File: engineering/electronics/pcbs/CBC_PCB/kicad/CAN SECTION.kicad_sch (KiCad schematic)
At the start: 44 parts, among them U25 ADM3053BRWZ-REEL7, U26 ADM3053BRWZ-REEL7, X1 8MHz, X2 8MHz

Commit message: electronics: integrate CBC PCB updates
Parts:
- C10, C11, C3, C6: symbol EasyEDA_Lib:CC0402JRNPO9BN220 -> CBC_PCB:CC0402JRNPO9BN220
- C12, C48, C49, C5, C53, C54: symbol EasyEDA_Lib:CL21A475KBQNNNE -> CBC_PCB:CL21A475KBQNNNE
- C13, C4, C47, C50, C51, C55, C56, C57: symbol EasyEDA_Lib:GRM21BR61H106KE43L -> CBC_PCB:GRM21BR61H106KE43L
- C14, C2, C52, C58: symbol EasyEDA_Lib:CC0402KRX7R7BB104 -> CBC_PCB:CC0402KRX7R7BB104
- C16, C17, C8, C9: symbol EasyEDA_Lib:GRM1555C1H221JA01D -> CBC_PCB:GRM1555C1H221JA01D
- D1, D2: symbol EasyEDA_Lib:NUP2105LT1G -> CBC_PCB:NUP2105LT1G
- H1, H2: symbol EasyEDA_Lib:PZ254V-11-02P -> CBC_PCB:PZ254V-11-02P
- L1, L2: symbol EasyEDA_Lib:ACT45B-510-2P-TF -> CBC_PCB:ACT45B-510-2P-TF
- R1, R4: symbol EasyEDA_Lib:0603WAF1200T5E -> CBC_PCB:0603WAF1200T5E
- R2, R3: symbol EasyEDA_Lib:RT0402BRD0710KL -> CBC_PCB:RT0402BRD0710KL
- R34, R35: symbol EasyEDA_Lib:RC0402FR-070RL -> CBC_PCB:RC0402FR-070RL
- U25, U26: symbol EasyEDA_Lib:ADM3053BRWZ-REEL7 -> CBC_PCB:ADM3053BRWZ-REEL7
- U3, U5: symbol EasyEDA_Lib:MCP2515T-I/ST -> CBC_PCB:MCP2515T-I/ST
- X1, X2: symbol EasyEDA_Lib:H1OEL89CSC-SUGYLC-8M -> CBC_PCB:H1OEL89CSC-SUGYLC-8M
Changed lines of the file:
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@@
 	)
 	(junction
-		(at 281.94 200.66)
-		(diameter 0)
-		(color 0 0 0 0)
-	)
-	(junction
 		(at 302.26 55.88)
 		(diameter 0)
@@
 	)
 	(junction
-		(at 266.7 64.77)
-		(diameter 0)
-		(color 0 0 0 0)
-	)
-	(junction
 		(at 57.15 74.93)
 		(diameter 0)
@@
 	(wire
 		(pts
-			(xy 266.7 64.77) (xy 261.62 64.77)
+			(xy 261.62 64.77) (xy 267.97 64.77)
 		)
 		(stroke
@@
 	(wire
 		(pts
-			(xy 267.97 64.77) (xy 266.7 64.77)
-		)
-		(stroke
-			(width 0)
-			(type default)
-		)
-	)
-	(wire
-		(pts
 			(xy 340.36 180.34) (xy 346.71 180.34)
 		)
@@
 	(wire
 		(pts
-			(xy 284.48 200.66) (xy 281.94 200.66)
-		)
-		(stroke
-			(width 0)
-			(type default)
-		)
-	)
-	(wire
-		(pts
 			(xy 283.21 194.31) (xy 288.29 194.31)
 		)
@@
 	(wire
 		(pts
-			(xy 281.94 200.66) (xy 278.13 200.66)
+			(xy 278.13 200.66) (xy 284.48 200.66)
 		)
 		(stroke
@@
 	)
 	(symbol
-		(lib_id "EasyEDA_Lib:GRM1555C1H221JA01D")
+		(lib_id "CBC_PCB:GRM1555C1H221JA01D")
 		(at 323.85 196.85 90)
 		(unit 1)
@@
 	)
 	(symbol
-		(lib_id "EasyEDA_Lib:ADM3053BRWZ-REEL7")
+		(lib_id "CBC_PCB:ADM3053BRWZ-REEL7")
 		(at 220.98 55.88 0)
 		(unit 1)
@@
 	)
 	(symbol
-		(lib_id "EasyEDA_Lib:CL21A475KBQNNNE")
+		(lib_id "CBC_PCB:CL21A475KBQNNNE")
 		(at 196.85 201.93 90)
 		(unit 1)
@@
 	)
 	(symbol
-		(lib_id "EasyEDA_Lib:GRM1555C1H221JA01D")
+		(lib_id "CBC_PCB:GRM1555C1H221JA01D")
 		(at 314.96 59.69 90)
 		(unit 1)
@@
 	)
 	(symbol
-		(lib_id "EasyEDA_Lib:H1OEL89CSC-SUGYLC-8M")
+		(lib_id "CBC_PCB:H1OEL89CSC-SUGYLC-8M")
 		(at 41.91 215.9 0)
 		(unit 1)
@@
 	)
 	(symbol
-		(lib_id "EasyEDA_Lib:0603WAF1200T5E")
+		(lib_id "CBC_PCB:0603WAF1200T5E")
 		(at 302.26 49.53 90)
 		(unit 1)
@@
 	)
 	(symbol
-		(lib_id "EasyEDA_Lib:RC0402FR-070RL")
+		(lib_id "CBC_PCB:RC0402FR-070RL")
 		(at 248.92 36.83 0)
 		(unit 1)
@@
 	)
 	(symbol
-		(lib_id "EasyEDA_Lib:GRM21BR61H106KE43L")
+		(lib_id "CBC_PCB:GRM21BR61H106KE43L")
 		(at 207.01 203.2 90)
 		(unit 1)
@@
 	)
 	(symbol
-		(lib_id "EasyEDA_Lib:H1OEL89CSC-SUGYLC-8M")
+		(lib_id "CBC_PCB:H1OEL89CSC-SUGYLC-8M")
 		(at 44.45 74.93 0)
 		(unit 1)
@@
 	)
 	(symbol
-		(lib_id "EasyEDA_Lib:RC0402FR-070RL")
+		(lib_id "CBC_PCB:RC0402FR-070RL")
 		(at 265.43 172.72 0)
 		(unit 1)
@@
 	)
 	(symbol
-		(lib_id "EasyEDA_Lib:NUP2105LT1G")
+		(lib_id "CBC_PCB:NUP2105LT1G")
 		(at 335.28 214.63 180)
 		(unit 1)
@@
 	)
 	(symbol
-		(lib_id "EasyEDA_Lib:CL21A475KBQNNNE")
+		(lib_id "CBC_PCB:CL21A475KBQNNNE")
 		(at 175.26 49.53 90)
 		(unit 1)
@@
 	)
 	(symbol
-		(lib_id "EasyEDA_Lib:ACT45B-510-2P-TF")
+		(lib_id "CBC_PCB:ACT45B-510-2P-TF")
 		(at 289.56 54.61 0)
 		(unit 1)
@@
 	)
 	(symbol
-		(lib_id "EasyEDA_Lib:CL21A475KBQNNNE")
+		(lib_id "CBC_PCB:CL21A475KBQNNNE")
 		(at 180.34 66.04 90)
 		(unit 1)
@@
 	)
 	(symbol
-		(lib_id "EasyEDA_Lib:CL21A475KBQNNNE")
+		(lib_id "CBC_PCB:CL21A475KBQNNNE")
 		(at 191.77 185.42 90)
 		(unit 1)
@@
 	)
 	(symbol
-		(lib_id "EasyEDA_Lib:GRM21BR61H106KE43L")
+		(lib_id "CBC_PCB:GRM21BR61H106KE43L")
 		(at 278.13 207.01 90)
 		(unit 1)
@@
 	)
 	(symbol
-		(lib_id "EasyEDA_Lib:NUP2105LT1G")
+		(lib_id "CBC_PCB:NUP2105LT1G")
 		(at 326.39 77.47 180)
 		(unit 1)
@@
 	)
 	(symbol
-		(lib_id "EasyEDA_Lib:0603WAF1200T5E")
+		(lib_id "CBC_PCB:0603WAF1200T5E")
 		(at 311.15 186.69 90)
 		(unit 1)
@@
 	)
 	(symbol
-		(lib_id "EasyEDA_Lib:PZ254V-11-02P")
+		(lib_id "CBC_PCB:PZ254V-11-02P")
 		(at 316.23 194.31 0)
 		(unit 1)
@@
 	)
 	(symbol
-		(lib_id "EasyEDA_Lib:PZ254V-11-02P")
+		(lib_id "CBC_PCB:PZ254V-11-02P")
 		(at 307.34 57.15 0)
 		(unit 1)
@@
 	)
 	(symbol
-		(lib_id "EasyEDA_Lib:GRM21BR61H106KE43L")
+		(lib_id "CBC_PCB:GRM21BR61H106KE43L")
 		(at 185.42 50.8 90)
 		(unit 1)
@@
 	)
 	(symbol
-		(lib_id "EasyEDA_Lib:GRM1555C1H221JA01D")
+		(lib_id "CBC_PCB:GRM1555C1H221JA01D")
 		(at 323.85 185.42 90)
 		(unit 1)
@@
 	)
 	(symbol
-		(lib_id "EasyEDA_Lib:GRM21BR61H106KE43L")
+		(lib_id "CBC_PCB:GRM21BR61H106KE43L")
 		(at 190.5 67.31 90)
 		(unit 1)
@@
 	)
 	(symbol
-		(lib_id "EasyEDA_Lib:GRM21BR61H106KE43L")
+		(lib_id "CBC_PCB:GRM21BR61H106KE43L")
 		(at 100.33 92.71 90)
 		(unit 1)
@@
 	(symbol
 		(lib_id "power:PWR_FLAG")
-		(at 311.15 191.77 0)
+		(at 311.15 191.77 90)
 		(unit 1)
 		(body_style 1)
@@
 		(fields_autoplaced yes)
 		(property "Reference" "#FLG058"
-			(at 311.15 190.5 0)
+			(at 309.88 191.77 0)
 			(hide yes)
 			(show_name no)
@@
 		)
 		(property "Value" "PWR_FLAG"
-			(at 311.15 186.69 0)
+			(at 306.07 191.77 0)
 			(hide yes)
 			(show_name no)
@@
 	)
 	(symbol
-		(lib_id "EasyEDA_Lib:CC0402KRX7R7BB104")
+		(lib_id "CBC_PCB:CC0402KRX7R7BB104")
 		(at 107.95 92.71 90)
 		(unit 1)
@@
 	)
 	(symbol
-		(lib_id "EasyEDA_Lib:CC0402JRNPO9BN220")
+		(lib_id "CBC_PCB:CC0402JRNPO9BN220")
 		(at 54.61 219.71 90)
 		(unit 1)
@@
 	)
 	(symbol
-		(lib_id "EasyEDA_Lib:CC0402JRNPO9BN220")
+		(lib_id "CBC_PCB:CC0402JRNPO9BN220")
 		(at 57.15 78.74 90)
 		(unit 1)
@@
 	)
 	(symbol
-		(lib_id "EasyEDA_Lib:CL21A475KBQNNNE")
+		(lib_id "CBC_PCB:CL21A475KBQNNNE")
 		(at 87.63 232.41 90)
 		(unit 1)
@@
 	)
 	(symbol
-		(lib_id "EasyEDA_Lib:CL21A475KBQNNNE")
+		(lib_id "CBC_PCB:CL21A475KBQNNNE")
 		(at 90.17 91.44 90)
 		(unit 1)
@@
 	)
 	(symbol
-		(lib_id "EasyEDA_Lib:GRM1555C1H221JA01D")
+		(lib_id "CBC_PCB:GRM1555C1H221JA01D")
 		(at 314.96 48.26 90)
 		(unit 1)
@@
 	)
 	(symbol
-		(lib_id "EasyEDA_Lib:MCP2515T-I/ST")
+		(lib_id "CBC_PCB:MCP2515T-I/ST")
 		(at 100.33 54.61 0)
 		(unit 1)
@@
 	)
 	(symbol
-		(lib_id "EasyEDA_Lib:MCP2515T-I/ST")
+		(lib_id "CBC_PCB:MCP2515T-I/ST")
 		(at 97.79 195.58 0)
 		(unit 1)
@@
 	)
 	(symbol
-		(lib_id "EasyEDA_Lib:GRM21BR61H106KE43L")
+		(lib_id "CBC_PCB:GRM21BR61H106KE43L")
 		(at 261.62 71.12 90)
 		(unit 1)
@@
 	)
 	(symbol
-		(lib_id "EasyEDA_Lib:RT0402BRD0710KL")
+		(lib_id "CBC_PCB:RT0402BRD0710KL")
 		(at 69.85 27.94 90)
 		(unit 1)
@@
 	)
 	(symbol
-		(lib_id "EasyEDA_Lib:CC0402KRX7R7BB104")
+		(lib_id "CBC_PCB:CC0402KRX7R7BB104")
 		(at 105.41 233.68 90)
 		(unit 1)
@@
 	)
 	(symbol
-		(lib_id "EasyEDA_Lib:CC0402KRX7R7BB104")
+		(lib_id "CBC_PCB:CC0402KRX7R7BB104")
 		(at 284.48 207.01 90)
 		(unit 1)
@@
 	)
 	(symbol
-		(lib_id "EasyEDA_Lib:RT0402BRD0710KL")
+		(lib_id "CBC_PCB:RT0402BRD0710KL")
 		(at 67.31 168.91 90)
 		(unit 1)
@@
 	)
 	(symbol
-		(lib_id "EasyEDA_Lib:CC0402JRNPO9BN220")
+		(lib_id "CBC_PCB:CC0402JRNPO9BN220")
 		(at 30.48 78.74 90)
 		(unit 1)
@@
 	)
 	(symbol
-		(lib_id "EasyEDA_Lib:GRM21BR61H106KE43L")
+		(lib_id "CBC_PCB:GRM21BR61H106KE43L")
 		(at 201.93 186.69 90)
 		(unit 1)
@@
 	)
 	(symbol
-		(lib_id "EasyEDA_Lib:GRM21BR61H106KE43L")
+		(lib_id "CBC_PCB:GRM21BR61H106KE43L")
 		(at 97.79 233.68 90)
 		(unit 1)
@@
 	)
 	(symbol
-		(lib_id "EasyEDA_Lib:ADM3053BRWZ-REEL7")
+		(lib_id "CBC_PCB:ADM3053BRWZ-REEL7")
 		(at 237.49 191.77 0)
 		(unit 1)
@@
 	)
 	(symbol
-		(lib_id "EasyEDA_Lib:CC0402KRX7R7BB104")
+		(lib_id "CBC_PCB:CC0402KRX7R7BB104")
 		(at 267.97 71.12 90)
 		(unit 1)
@@
 	)
 	(symbol
-		(lib_id "EasyEDA_Lib:CC0402JRNPO9BN220")
+		(lib_id "CBC_PCB:CC0402JRNPO9BN220")
 		(at 27.94 219.71 90)
 		(unit 1)
@@
 	)
 	(symbol
-		(lib_id "EasyEDA_Lib:ACT45B-510-2P-TF")
+		(lib_id "CBC_PCB:ACT45B-510-2P-TF")
 		(at 298.45 191.77 0)
 		(unit 1)

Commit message: electronics: update CBC PCB and crystal parts
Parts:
- X1, X2: value 8MHz -> 16MHz; footprint EasyEDA_Lib:HC-49S_L11.5-W4.7-P4.88 -> EasyEDA_Lib:CRYSTAL-SMD_L3.2-W2.5_3225-8MHZ; LCSC Part Name HC-49US 8MHZ 20PF ±20PPM -20~70°C (±30PPM) -> 16MHz ±50ppm 8pF; Manufacturer YXC(扬兴晶振) -> NDK; Manufacturer Part H1OEL89CSC-SUGYLC-8M -> NX3225GB-16MHZ-STD-CRA-2; Supplier Part C7471633 -> C481399
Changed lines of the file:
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@@
 			)
 		)
-		(property "Value" "8MHz"
+		(property "Value" "16MHz"
 			(at 41.91 219.71 0)
 			(show_name no)
@@
 			)
 		)
-		(property "Footprint" "EasyEDA_Lib:HC-49S_L11.5-W4.7-P4.88"
+		(property "Footprint" "EasyEDA_Lib:CRYSTAL-SMD_L3.2-W2.5_3225-8MHZ"
 			(at 41.91 215.9 0)
 			(hide yes)
@@
 			)
 		)
-		(property "Datasheet" "https://item.szlcsc.com/datasheet/H1OEL89CSC-SUGYLC-8M/8526929.html"
+		(property "Datasheet" "https://item.szlcsc.com/datasheet/NX3225GB-16MHZ-STD-CRA-2/489116.html"
 			(at 41.91 215.9 0)
 			(hide yes)
@@
 			)
 		)
-		(property "Description" "Type:Through Hole Crystal Oscillator Frequency:8MHz Normal temperature Frequency Tolerance:±20ppm Normal temperature Frequency Tolerance:±20ppm Load Capacitance:20pF Frequency Stability:±30ppm Frequency Stability:±30ppm Operating Temperature:-20°C~+70°C Ope"
+		(property "Description" "Frequency:16MHz Normal temperature Frequency Tolerance:±50ppm Load Capacitance:8pF Frequency Stability:±150ppm Equivalent Series Resistance(ESR):120Ω Operating Temperature:-40℃~+150℃"
 			(at 41.91 215.9 0)
 			(hide yes)
@@
 			)
 		)
-		(property "Manufacturer Part" "H1OEL89CSC-SUGYLC-8M"
+		(property "Manufacturer Part" "NX3225GB-16MHZ-STD-CRA-2"
 			(at 41.91 215.9 0)
 			(hide yes)
@@
 			)
 		)
-		(property "Manufacturer" "YXC(扬兴晶振)"
+		(property "Manufacturer" "NDK"
 			(at 41.91 215.9 0)
 			(hide yes)
@@
 			)
 		)
-		(property "Supplier Part" "C7471633"
+		(property "Supplier Part" "C481399"
 			(at 41.91 215.9 0)
 			(hide yes)
@@
 			)
 		)
-		(property "LCSC Part Name" "HC-49US 8MHZ 20PF ±20PPM -20~70°C (±30PPM)"
+		(property "LCSC Part Name" "16MHz ±50ppm 8pF"
 			(at 41.91 215.9 0)
 			(hide yes)
@@
 			)
 		)
-		(property "Value" "8MHz"
+		(property "Value" "16MHz"
 			(at 44.45 78.74 0)
 			(show_name no)
@@
 			)
 		)
-		(property "Footprint" "EasyEDA_Lib:HC-49S_L11.5-W4.7-P4.88"
+		(property "Footprint" "EasyEDA_Lib:CRYSTAL-SMD_L3.2-W2.5_3225-8MHZ"
 			(at 44.45 74.93 0)
 			(hide yes)
@@
 			)
 		)
-		(property "Datasheet" "https://item.szlcsc.com/datasheet/H1OEL89CSC-SUGYLC-8M/8526929.html"
+		(property "Datasheet" "https://item.szlcsc.com/datasheet/NX3225GB-16MHZ-STD-CRA-2/489116.html"
 			(at 44.45 74.93 0)
 			(hide yes)
@@
 			)
 		)
-		(property "Description" "Type:Through Hole Crystal Oscillator Frequency:8MHz Normal temperature Frequency Tolerance:±20ppm Normal temperature Frequency Tolerance:±20ppm Load Capacitance:20pF Frequency Stability:±30ppm Frequency Stability:±30ppm Operating Temperature:-20°C~+70°C Ope"
+		(property "Description" "Frequency:16MHz Normal temperature Frequency Tolerance:±50ppm Load Capacitance:8pF Frequency Stability:±150ppm Equivalent Series Resistance(ESR):120Ω Operating Temperature:-40℃~+150℃"
 			(at 44.45 74.93 0)
 			(hide yes)
@@
 			)
 		)
-		(property "Manufacturer Part" "H1OEL89CSC-SUGYLC-8M"
+		(property "Manufacturer Part" "NX3225GB-16MHZ-STD-CRA-2"
 			(at 44.45 74.93 0)
 			(hide yes)
@@
 			)
 		)
-		(property "Manufacturer" "YXC(扬兴晶振)"
+		(property "Manufacturer" "NDK"
 			(at 44.45 74.93 0)
 			(hide yes)
@@
 			)
 		)
-		(property "Supplier Part" "C7471633"
+		(property "Supplier Part" "C481399"
 			(at 44.45 74.93 0)
 			(hide yes)
@@
 			)
 		)
-		(property "LCSC Part Name" "HC-49US 8MHZ 20PF ±20PPM -20~70°C (±30PPM)"
+		(property "LCSC Part Name" "16MHz ±50ppm 8pF"
 			(at 44.45 74.93 0)
 			(hide yes)

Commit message: electronics: update CMAIN and CBC PCB files
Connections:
- net GND_CB is gone; now on net GND: C16.1, C17.2, C57.1, C58.1, D2.3, R35.2, U26.11 (GND2), U26.13 (GND2), U26.16 (GND2), U26.20 (GND2)
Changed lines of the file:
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@@
 			)
 		)
-		(property "Value" "GND_CB"
+		(property "Value" "GND"
 			(at 285.75 215.9 0)
 			(show_name no)
@@
 			)
 		)
-		(property "Value" "GND_CB"
+		(property "Value" "GND"
 			(at 276.86 215.9 0)
 			(show_name no)
@@
 			)
 		)
-		(property "Value" "GND_CB"
+		(property "Value" "GND"
 			(at 332.74 195.58 0)
 			(show_name no)
@@
 			)
 		)
-		(property "Value" "GND_CB"
+		(property "Value" "GND"
 			(at 331.47 231.14 0)
 			(show_name no)
@@
 			)
 		)
-		(property "Value" "GND_CB"
+		(property "Value" "GND"
 			(at 262.89 207.01 0)
 			(show_name no)
@@
 			)
 		)
-		(property "Value" "GND_CB"
+		(property "Value" "GND"
 			(at 270.51 176.53 0)
 			(show_name no)

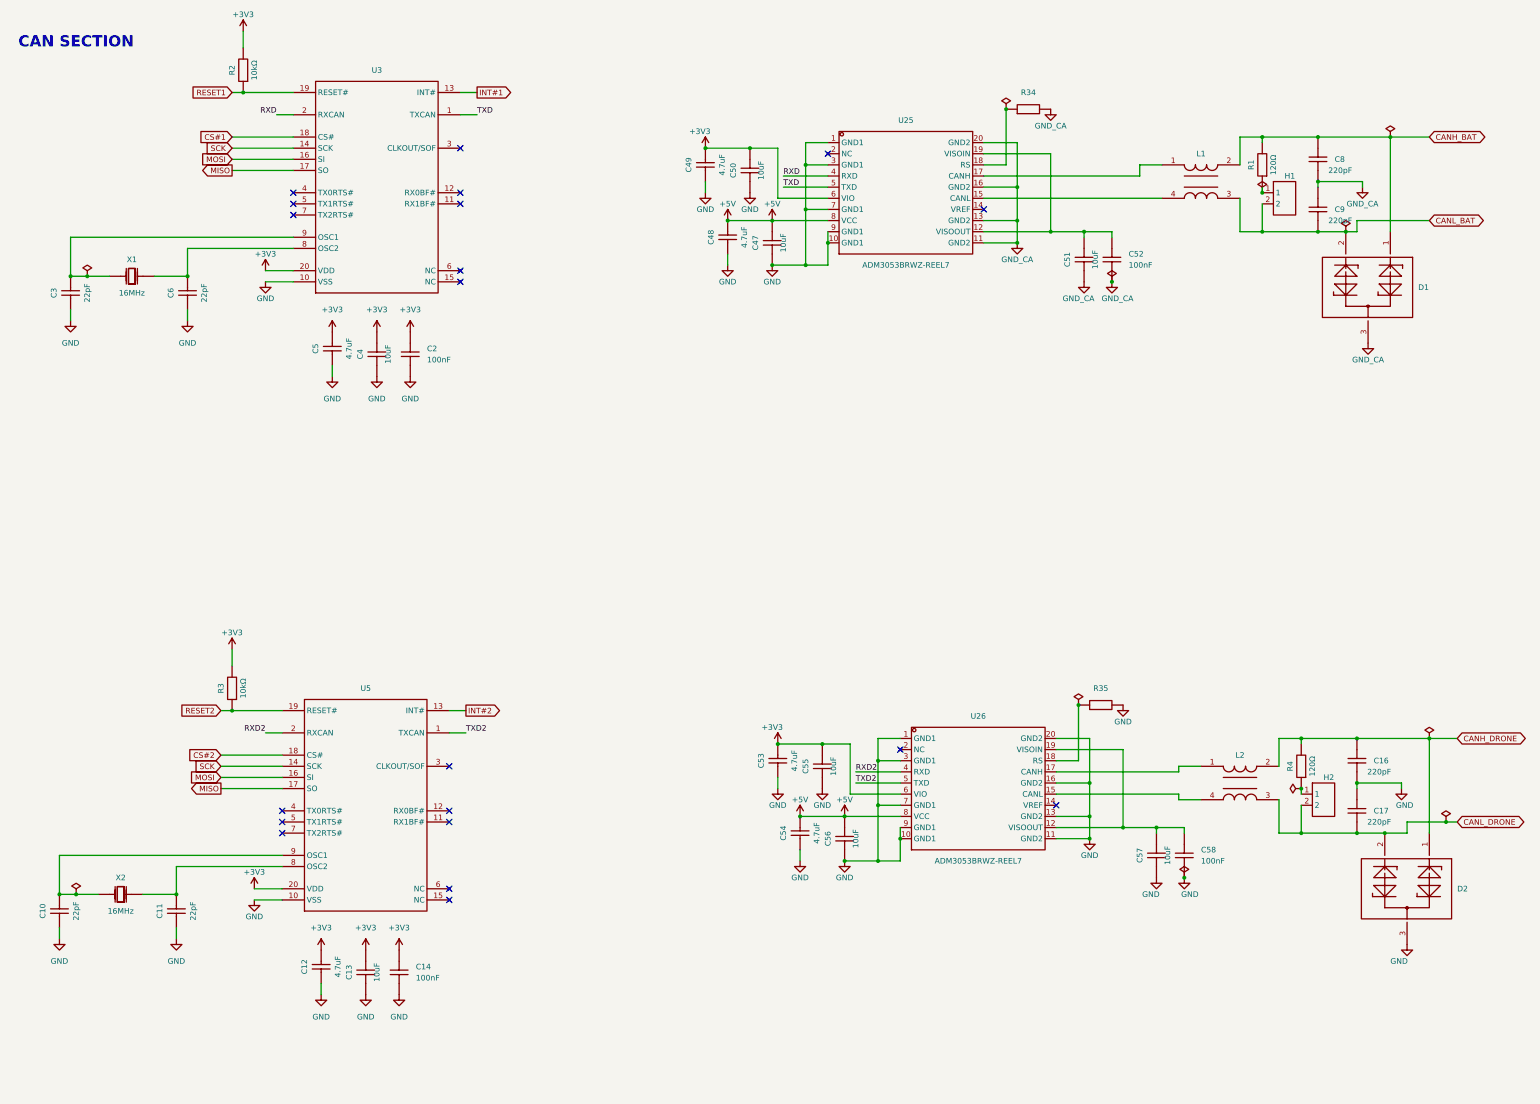
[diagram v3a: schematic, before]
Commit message: pcb: update CBC import and routing rules
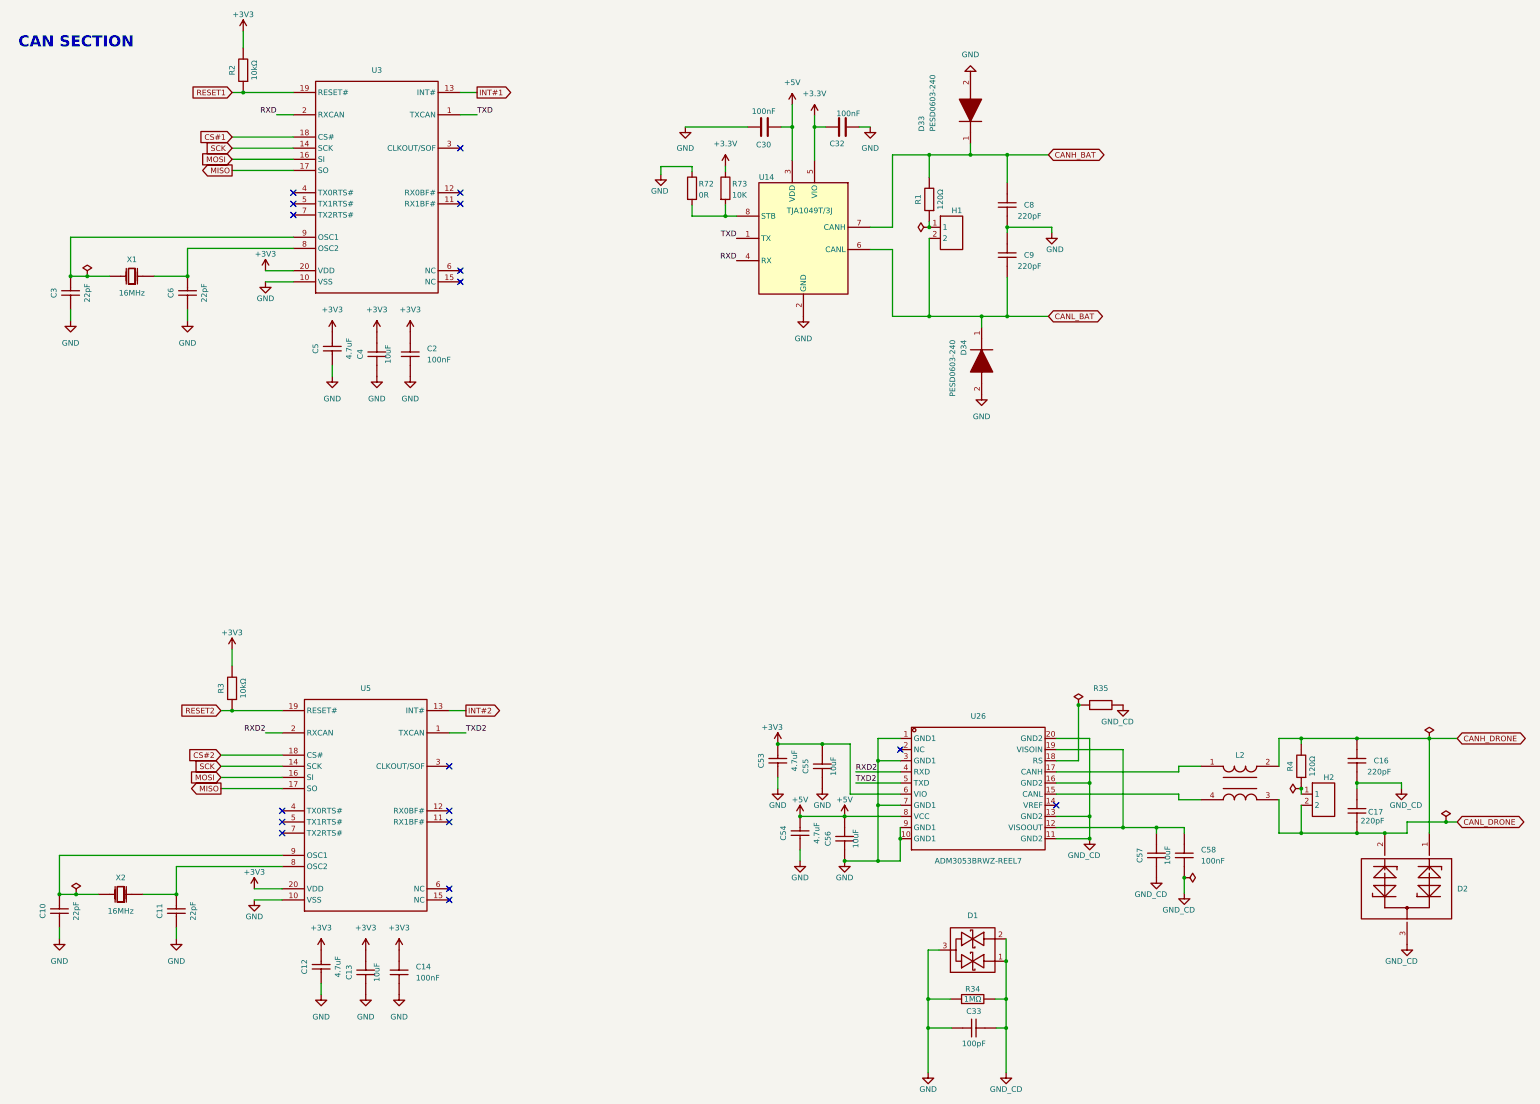
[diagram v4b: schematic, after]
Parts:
- removed C47, C50, C51: 10uF, EasyEDA_Lib:C0805, symbol CBC_PCB:GRM21BR61H106KE43L
- removed C48, C49: 4.7uF, EasyEDA_Lib:C0805, symbol CBC_PCB:CL21A475KBQNNNE
- removed C52: 100nF, EasyEDA_Lib:C0402, symbol CBC_PCB:CC0402KRX7R7BB104
- removed D1: (no value), EasyEDA_Lib:SOT-23-3_L2.9-W1.3-P1.90-LS2.4-BL-2, symbol CBC_PCB:NUP2105LT1G
- removed L1: (no value), EasyEDA_Lib:FILTER-SMD_4P-L4.5-W3.2_ACT45B-510-2P, symbol CBC_PCB:ACT45B-510-2P-TF
- removed R34: 0Ω, EasyEDA_Lib:R0402, symbol CBC_PCB:RC0402FR-070RL
- removed U25: ADM3053BRWZ-REEL7, EasyEDA_Lib:SOIC-20_L13.0-W7.6-P1.27-LS10.3-BL, symbol CBC_PCB:ADM3053BRWZ-REEL7
- added C30, C32: 100nF, Capacitor_SMD:C_0805_2012Metric_Pad1.18x1.45mm_HandSolder, symbol Device:C
- added C33: 100pF, EasyEDA_Lib_2:C0805, symbol EasyEDA_Lib_2:C0805C101J2GAC7800
- added D1: (no value), EasyEDA_Lib_2:SOT-323-3_L2.0-W1.3-P1.30-LS2.1-BR, symbol EasyEDA_Lib_2:PESD1CAN-UX
- added D33, D34: PESD0603-240, Samacsys:DIONC1608X55N, symbol Samacsys_kicad_sym:PESD0603-240
- added R34: 1MΩ, EasyEDA_Lib_2:R0805, symbol EasyEDA_Lib_2:RC0805FR-071ML
- added R72: 0R, Resistor_SMD:R_0805_2012Metric_Pad1.20x1.40mm_HandSolder, symbol Device:R
- added R73: 10K, Resistor_SMD:R_0805_2012Metric_Pad1.20x1.40mm_HandSolder, symbol Device:R
- added U14: TJA1049T/3J, Samacsys:SOIC127P600X175-8N, symbol Samacsys_kicad_sym:TJA1049T_3J
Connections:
- net GND_CA is gone; now on net GND: C8.1, C9.2
- net +5V: now also C30.2, U14.3 (VDD)
- net CANH_BAT: now also D33.1 (K), U14.7 (CANH)
- net CANL_BAT: now also D34.1 (K), U14.6 (CANL)
- net GND: now also C30.1, C32.2, C33.1, D1.3, D33.2 (A), D34.2 (A), R34.1, R72.1, U14.2 (GND); no longer C16.1, C17.2, C57.1, C58.1, D2.3, R35.2, U26.11 (GND2), U26.13 (GND2), U26.16 (GND2), U26.20 (GND2)
- net RXD: now also U14.4 (RX)
- net TXD: now also U14.1 (TX)
- new net: R72.2, R73.2, U14.8 (STB)
- new net +3.3V: C32.1, R73.1, U14.5 (VIO)
- new net GND_CD: C16.1, C17.2, C33.2, C57.1, C58.1, D1.1, D1.2, D2.3, R34.2, R35.2, U26.11 (GND2), U26.13 (GND2), U26.16 (GND2), U26.20 (GND2)
- no-connect marks 20 -> 18
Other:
- moved on the sheet: C8, C9, H1, R1
